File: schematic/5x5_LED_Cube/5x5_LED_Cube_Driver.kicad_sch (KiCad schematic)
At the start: 26 parts, among them J1 Layers, J2 Adafruit_Micro_SD_Card_SPI_SD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, J3 Display, Q1 DMG2305UX, Q2 DMG2305UX, Q3 DMG2305UX, Q4 DMG2305UX, Q5 DMG2305UX, SW1 RotaryEncoder_Switch, SW2 SW_SPDT, U1 TLC5940NT, U2 TLC5940NT, U3 Pico

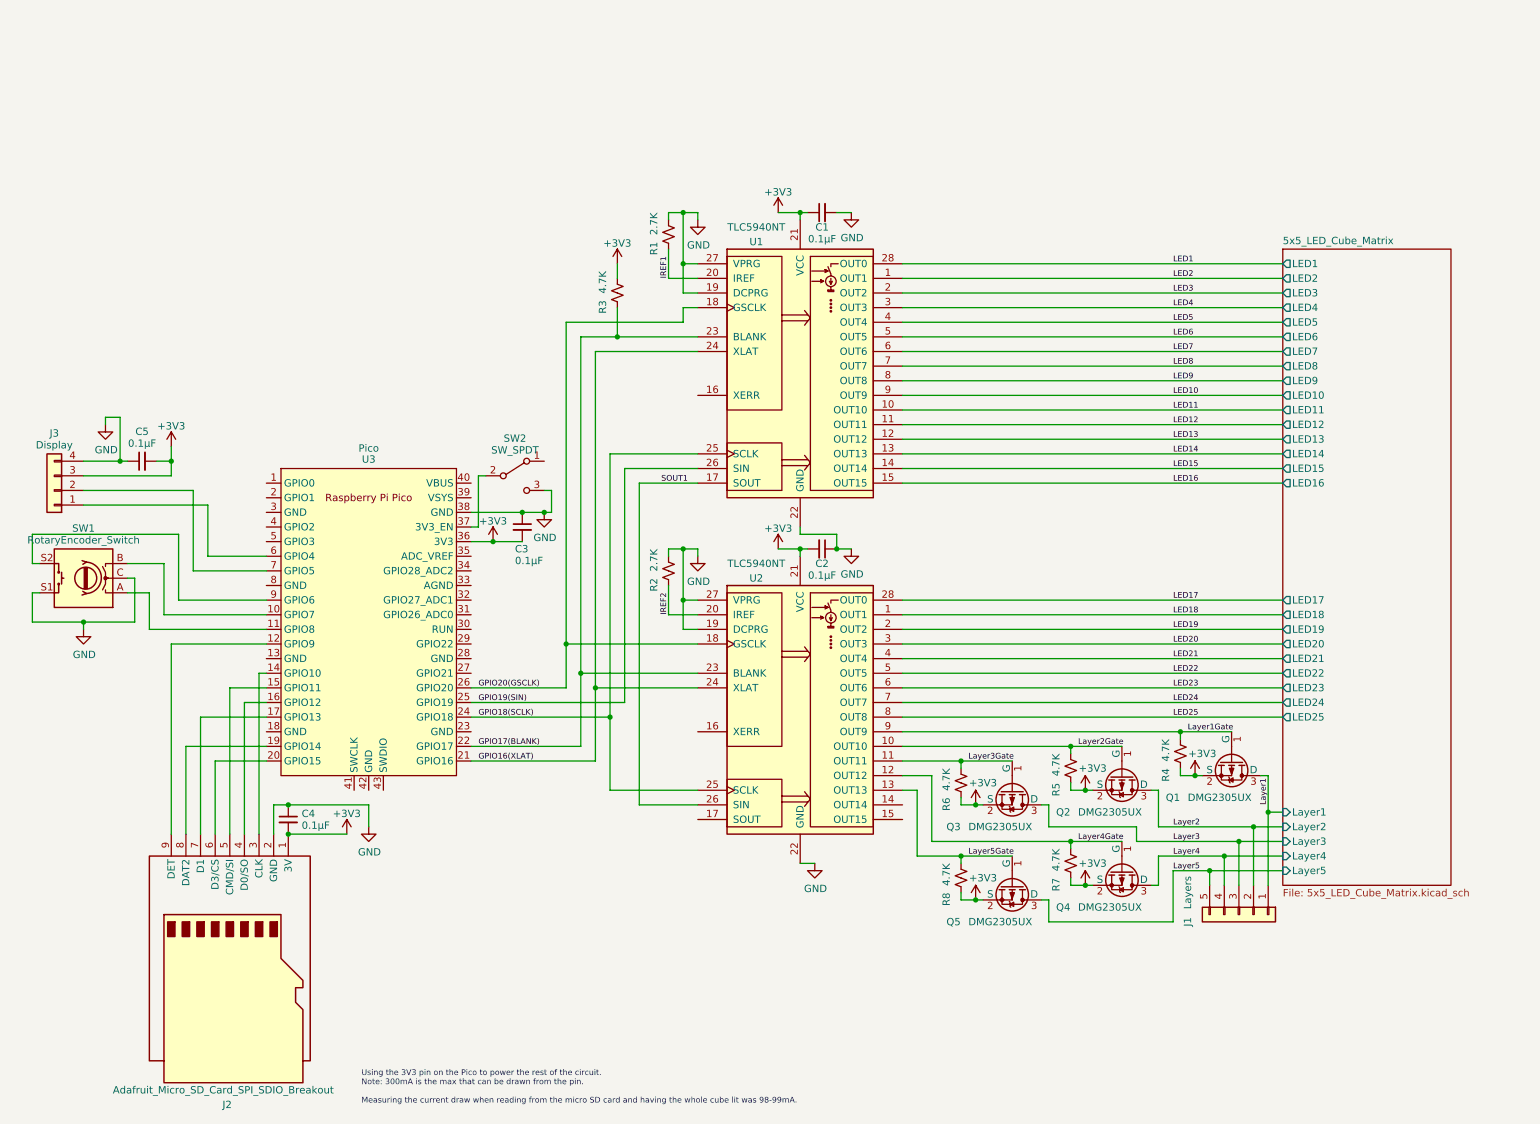
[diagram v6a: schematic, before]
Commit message: Updated schematic for 5x5 cube to use new symbol/footprint for oled display
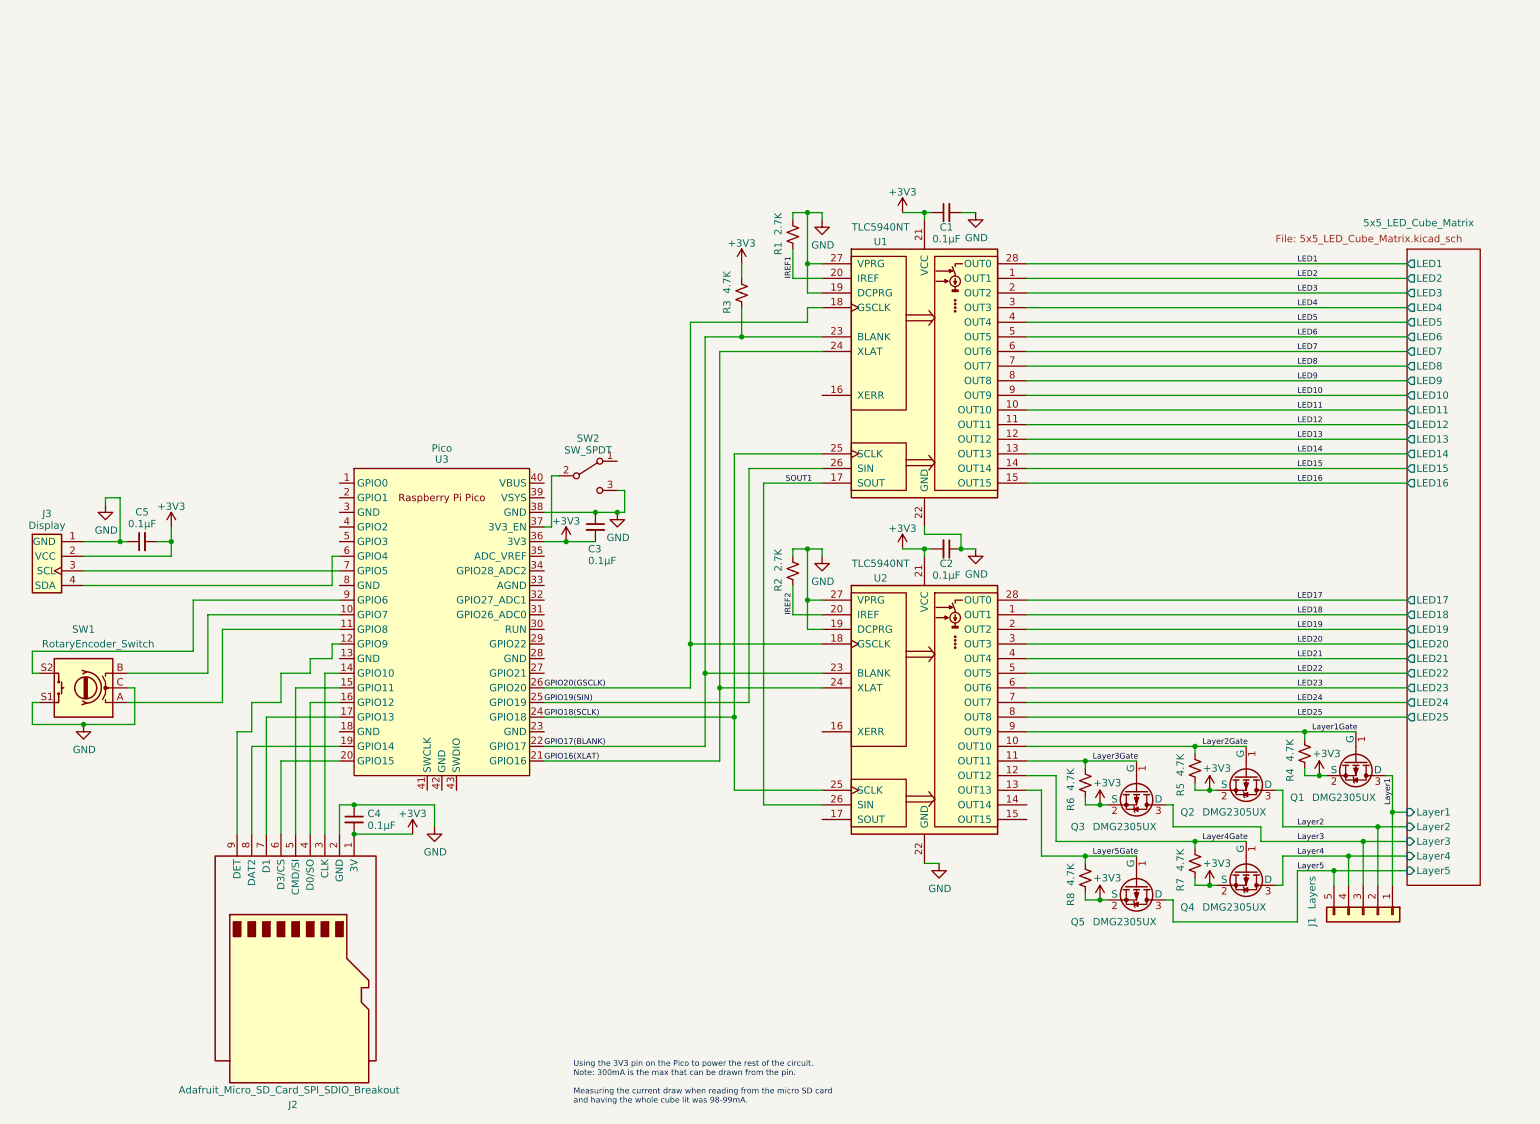
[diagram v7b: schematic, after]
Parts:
- J3: footprint (none) -> My_Library:0.96 Inch OLED Module 12864 128x64 IIC I2C; symbol Connector_Generic:Conn_01x04 -> My_Library:0.96 Inch OLED Module 12864 128x64 IIC I2C
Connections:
- net +3V3: now also J3.2 (VCC); no longer J3.3 (Pin_3)
- net GND: now also J3.1 (GND); no longer J3.4 (Pin_4)
- net at U3.6 (GPIO4): now also J3.4 (SDA); no longer J3.1 (Pin_1)
- net at U3.7 (GPIO5): now also J3.3 (SCL); no longer J3.2 (Pin_2)
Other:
- moved on the sheet: C1, C2, C3, C4, C5, J1, J2, Q1, Q2, Q3, Q4, Q5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
